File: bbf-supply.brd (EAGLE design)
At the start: 21.6 x 54.6 mm, 18 parts, among them IC1 780X, IC2 LT1054, IC3 790X

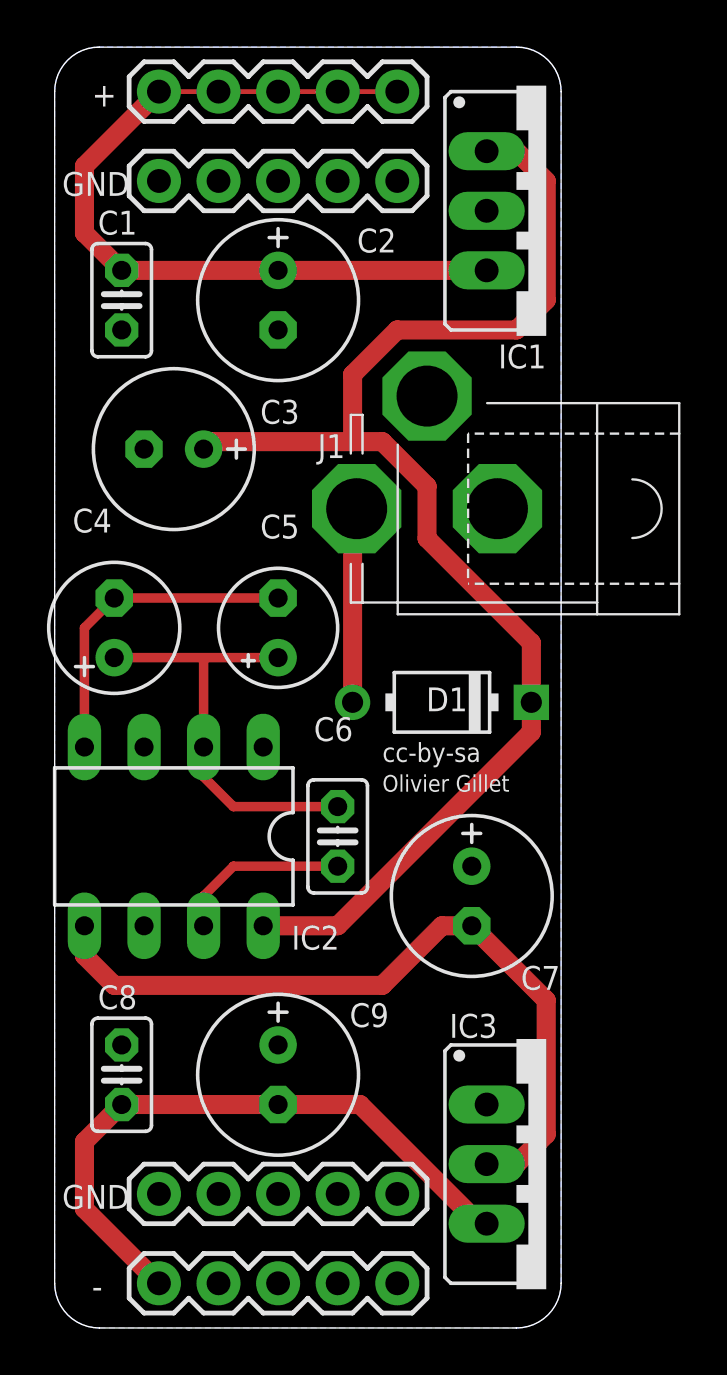
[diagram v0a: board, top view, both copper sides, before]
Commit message: supply more wider
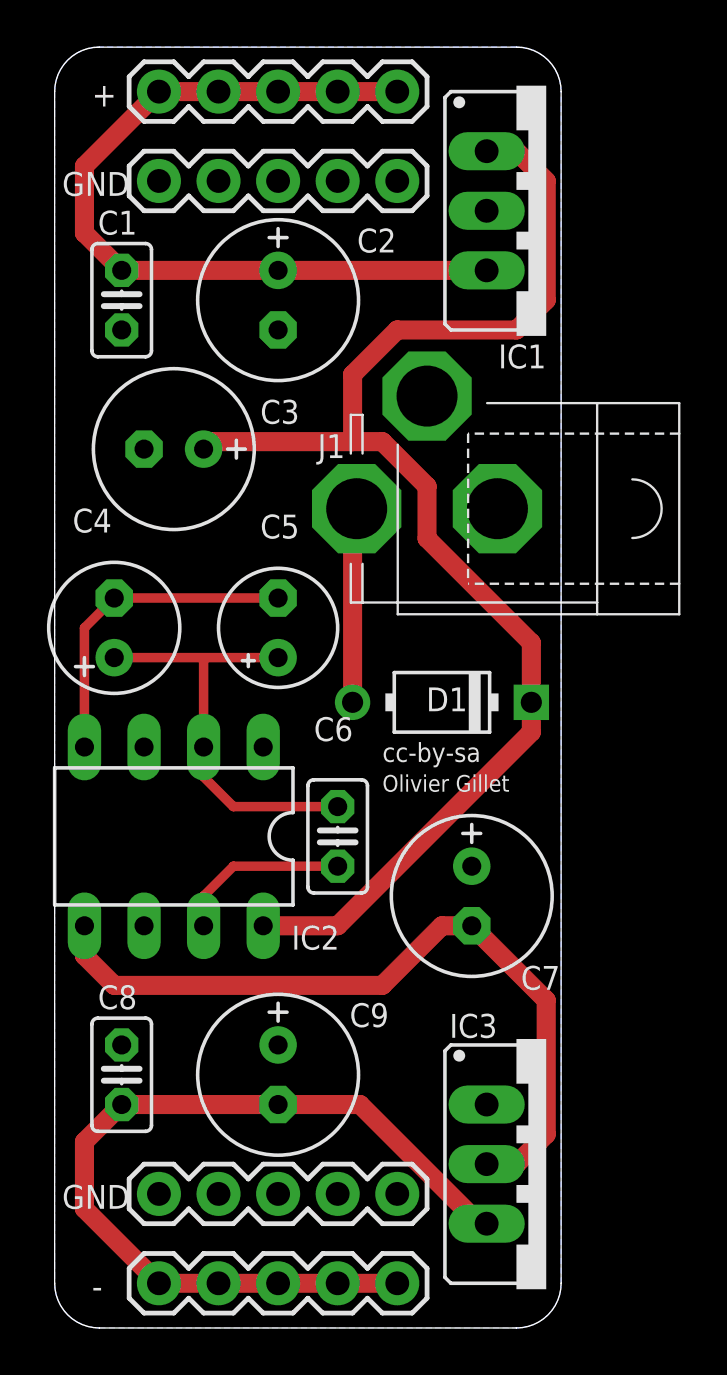
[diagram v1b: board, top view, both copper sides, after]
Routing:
- net VEE: track 27.3 -> 37.4 mm
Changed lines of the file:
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@@
 <contactref element="JP3" pad="3"/>
 <contactref element="JP3" pad="2"/>
-<wire x1="12.7" y1="58.42" x2="15.24" y2="58.42" width="0.2032" layer="1"/>
-<wire x1="15.24" y1="58.42" x2="17.78" y2="58.42" width="0.2032" layer="1"/>
-<wire x1="17.78" y1="58.42" x2="20.32" y2="58.42" width="0.2032" layer="1"/>
-<wire x1="20.32" y1="58.42" x2="22.86" y2="58.42" width="0.2032" layer="1"/>
+<wire x1="12.7" y1="58.42" x2="15.24" y2="58.42" width="0.8128" layer="1"/>
+<wire x1="15.24" y1="58.42" x2="17.78" y2="58.42" width="0.8128" layer="1"/>
+<wire x1="17.78" y1="58.42" x2="20.32" y2="58.42" width="0.8128" layer="1"/>
+<wire x1="20.32" y1="58.42" x2="22.86" y2="58.42" width="0.8128" layer="1"/>
 </signal>
 <signal name="N$44">
@@
 <contactref element="JP6" pad="3"/>
 <contactref element="JP6" pad="2"/>
-<wire x1="22.86" y1="7.62" x2="11.1125" y2="15.24" width="0" layer="19" extent="1-1"/>
-<wire x1="20.32" y1="7.62" x2="22.86" y2="7.62" width="0" layer="19" extent="1-1"/>
-<wire x1="17.78" y1="7.62" x2="20.32" y2="7.62" width="0" layer="19" extent="1-1"/>
-<wire x1="15.24" y1="7.62" x2="17.78" y2="7.62" width="0" layer="19" extent="1-1"/>
-<wire x1="12.7" y1="7.62" x2="15.24" y2="7.62" width="0" layer="19" extent="1-1"/>
+<wire x1="12.7" y1="7.62" x2="15.24" y2="7.62" width="0.8128" layer="1"/>
+<wire x1="15.24" y1="7.62" x2="17.78" y2="7.62" width="0.8128" layer="1"/>
+<wire x1="17.78" y1="7.62" x2="20.32" y2="7.62" width="0.8128" layer="1"/>
+<wire x1="20.32" y1="7.62" x2="22.86" y2="7.62" width="0.8128" layer="1"/>
 </signal>
 <signal name="N$58">

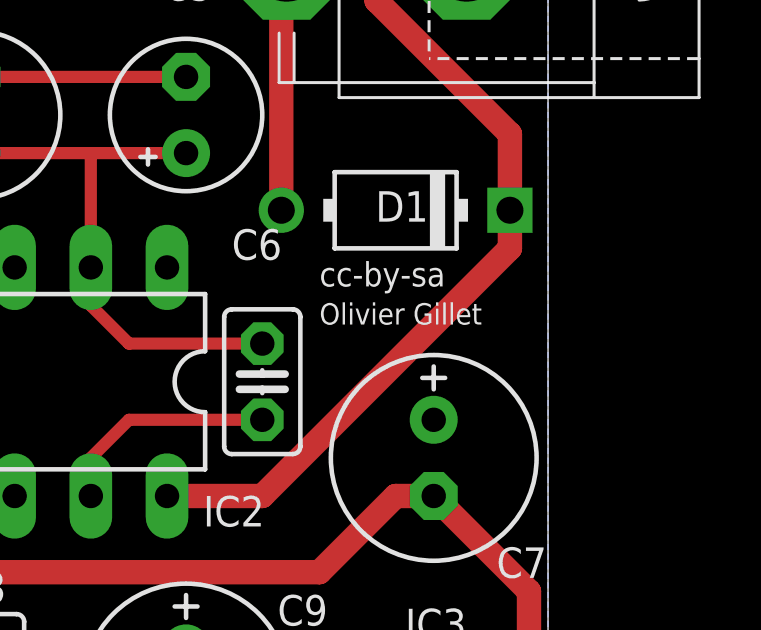
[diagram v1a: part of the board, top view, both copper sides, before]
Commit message: update names on boards and schematics
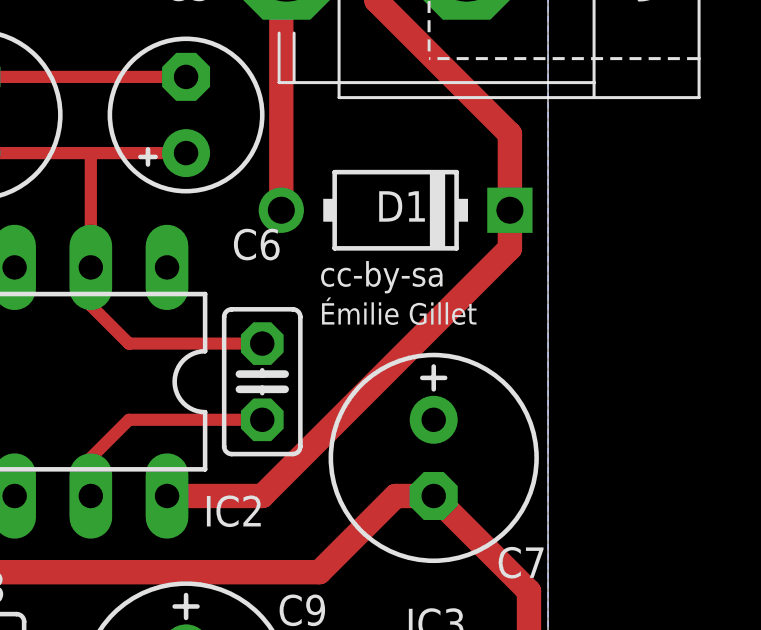
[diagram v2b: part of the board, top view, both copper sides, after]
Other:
- board text added: "Émilie Gillet"
- board text removed: "Olivier Gillet"
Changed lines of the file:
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@@
 <text x="8.5725" y="53.975" size="1.016" layer="25" ratio="15">GND</text>
 <text x="22.225" y="29.845" size="0.8128" layer="25" ratio="15">cc-by-sa</text>
-<text x="22.225" y="28.575" size="0.7112" layer="25" ratio="15">Olivier Gillet</text>
+<text x="22.225" y="28.575" size="0.7112" layer="25" ratio="15">Émilie Gillet</text>
 </plain>
 <attributes>
